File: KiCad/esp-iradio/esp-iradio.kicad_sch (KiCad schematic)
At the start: 0 parts

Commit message: KiCad: schematic on one A3 sheet in Elektuur style
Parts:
- added C1, C10, C12, C14, C22, C3, C5: 10uF, Capacitor_SMD:C_0805_2012Metric, symbol Elektuur:C
- added C11, C13, C17, C20, C21, C4, C6, C7, C8, C9: 100nF, Capacitor_SMD:C_0603_1608Metric, symbol Elektuur:C
- added C15, C16: 2.2uF, Capacitor_SMD:C_0603_1608Metric, symbol Elektuur:C
- added C18, C19: 2.2nF, Capacitor_SMD:C_0603_1608Metric, symbol Elektuur:C
- added C2, C23: 1uF, Capacitor_SMD:C_0603_1608Metric, symbol Elektuur:C
- added C24: 220uF 10V, Capacitor_SMD:CP_Elec_6.3x7.7, symbol Elektuur:C-polar
- added D1: SMAJ5.0CA, Diode_SMD:D_SMA, symbol Device:D_TVS
- added F1: 2A hold, Fuse:Fuse_1206_3216Metric, symbol Device:Polyfuse
- added FB1: 600R@100MHz, Inductor_SMD:L_0805_2012Metric, symbol Elektuur:L
- added FB2: 600R@100MHz 2A, Inductor_SMD:L_0805_2012Metric, symbol Elektuur:L
- added H1, H2, H3, H4: M3, MountingHole:MountingHole_3.2mm_M3, symbol Mechanical:MountingHole
- added J3: LCD 1.69in ST7789 (GND VCC SCL SDA RES DC CS BLK), Connector_PinSocket_2.54mm:PinSocket_1x08_P2.54mm_Vertical, symbol Connector_Generic:Conn_01x08
- added J4: microSD push-push, Connector_Card:microSD_HC_Hirose_DM3AT-SF-PEJM5, symbol Connector:Micro_SD_Card
- added J5: Line out 3.5mm, Connector_Audio:Jack_3.5mm_PJ320D_Horizontal, symbol Connector_Audio:AudioJack3
- added J6: Speaker 4-8 Ohm, Connector_JST:JST_PH_B2B-PH-K_1x02_P2.00mm_Vertical, symbol Connector_Generic:Conn_01x02
- added J7: USB-C power (GCT USB4125), Connector_USB:USB_C_Receptacle_GCT_USB4125-xx-x_6P_TopMnt_Horizontal, symbol Connector:USB_C_Receptacle_PowerOnly_6P
- added J8: Spare inputs, Connector_PinHeader_2.54mm:PinHeader_1x05_P2.54mm_Vertical, symbol Connector_Generic:Conn_01x05
- added MOD1: Olimex ESP32-DevKit-LiPo, esp-iradio:Olimex_ESP32-DevKit-LiPo_Socket, symbol esp-iradio:Olimex_ESP32-DevKit-LiPo
- added R1, R2: 5.1k 1%, Resistor_SMD:R_0603_1608Metric, symbol Elektuur:R
- added R10, R11, R12, R15, R3, R4, R5, R6, R7: 10k, Resistor_SMD:R_0603_1608Metric, symbol Elektuur:R
- added R13, R14: 10k DNP, Resistor_SMD:R_0603_1608Metric, symbol Elektuur:R
- added R16, R17: 470R, Resistor_SMD:R_0603_1608Metric, symbol Elektuur:R
- added R18, R19: 180k, Resistor_SMD:R_0603_1608Metric, symbol Elektuur:R
- added R20: 91k, Resistor_SMD:R_0603_1608Metric, symbol Elektuur:R
- added R21: 100k, Resistor_SMD:R_0603_1608Metric, symbol Elektuur:R
- added R8, R9: 0R, Resistor_SMD:R_0603_1608Metric, symbol Elektuur:R
- added SW1: EC11 with switch, Rotary_Encoder:RotaryEncoder_Alps_EC11E-Switch_Vertical_H20mm, symbol Device:RotaryEncoder_Switch
- added TP1: +5V_USBC, TestPoint:TestPoint_Pad_D1.5mm, symbol Connector:TestPoint
- added TP2: +VAMP, TestPoint:TestPoint_Pad_D1.5mm, symbol Connector:TestPoint
- added TP3: GND, TestPoint:TestPoint_Pad_D1.5mm, symbol Connector:TestPoint
- added TP4: +3V3, TestPoint:TestPoint_Pad_D1.5mm, symbol Connector:TestPoint
- added TP5: SPI_SCK, TestPoint:TestPoint_Pad_D1.5mm, symbol Connector:TestPoint
- added TP6: I2S_BCK, TestPoint:TestPoint_Pad_D1.5mm, symbol Connector:TestPoint
- added TP7: I2S_LRCK, TestPoint:TestPoint_Pad_D1.5mm, symbol Connector:TestPoint
- added TP8: I2S_DATA, TestPoint:TestPoint_Pad_D1.5mm, symbol Connector:TestPoint
- added U1: PCM5102APWR, Package_SO:TSSOP-20_4.4x6.5mm_P0.65mm, symbol Audio:PCM5102A
- added U2: PAM8302AASCR, Package_SO:SOIC-8_3.9x4.9mm_P1.27mm, symbol Amplifier_Audio:PAM8302AAS
- added U3: LM66100DCK, Package_TO_SOT_SMD:SOT-363_SC-70-6, symbol Power_Management:LM66100DCK
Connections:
- new net: MOD1.12 (IO14), TP7.1, U1.15 (LRCK)
- new net: J3.3 (Pin_3), J4.5 (CLK), R8.2 (-)
- new net: J3.4 (Pin_4), J4.3 (CMD), R9.2 (-)
- new net: J3.5 (Pin_5), MOD1.25 (IO21)
- new net: J3.6 (Pin_6), MOD1.22 (IO22)
- new net: J3.7 (Pin_7), MOD1.29 (IO5), R3.1 (+)
- new net: J3.8 (Pin_8), MOD1.10 (IO26)
- new net: J4.7 (DAT0), MOD1.27 (IO19), R5.1 (+)
- new net: C21.1 (+), R20.1 (+)
- new net: C6.1 (+), MOD1.7 (IO32), R10.2 (-), SW1.A
- new net: D1.2 (A2), F1.1, J7.A9 (VBUS), J7.B9 (VBUS)
- new net: MOD1.15 (IO13), TP8.1, U1.14 (DIN)
- new net: MOD1.28 (IO18), R8.1 (+), TP5.1
- new net: C7.1 (+), MOD1.8 (IO33), R11.2 (-), SW1.B
- new net: C8.1 (+), MOD1.9 (IO25), R12.2 (-), SW1.S1
- new net: MOD1.11 (IO27), TP6.1, U1.13 (BCK)
- new net: C19.1 (+), J5.R, R17.2 (-), R19.1 (+)
- new net: C18.1 (+), J5.T, R16.2 (-), R18.1 (+)
- new net: C15.1 (+), U1.2 (CAPP)
- new net: C15.2 (-), U1.4 (CAPM)
- new net: J4.1 (DAT2), R7.2 (-)
- new net: R15.2 (-), U1.17 (XSMT)
- new net: C17.1 (+), U1.18 (LDOO)
- new net: C16.1 (+), U1.5 (VNEG)
- new net: R16.1 (+), U1.6 (OUTL)
- new net: R17.1 (+), U1.7 (OUTR)
- new net: C20.1 (+), R18.2 (-), R19.2 (-)
- new net: MOD1.34 (IO2), R21.1 (+), U2.1 (~{SD})
- new net: C20.2 (-), U2.3 (IN+)
- new net: R20.2 (-), U2.4 (IN-)
- new net: J6.1 (Pin_1), U2.5 (OUT+)
- new net: J6.2 (Pin_2), U2.8 (OUT-)
- new net: J7.A5 (CC1), R1.1 (+)
- new net: J7.B5 (CC2), R2.1 (+)
- new net: J4.8 (DAT1), R6.1 (+)
- new net: MOD1.21 (IO23), R9.1 (+)
- new net: J4.2 (DAT3/CD), MOD1.32 (IO4), R4.2 (-)
- new net: J8.2 (Pin_2), MOD1.5 (IO34), R13.1 (+)
- new net: J8.3 (Pin_3), MOD1.3 (IO36), R14.2 (-)
- new net +3V3: C10.1 (+), C11.1 (+), C12.1 (+), C3.1 (+), C4.1 (+), C5.1 (+), C9.1 (+), FB1.1 (+), J3.2 (Pin_2), J4.4 (VDD), J8.1 (Pin_1), MOD1.1 (3V3), R10.1 (+), R11.1 (+), R12.1 (+), R13.2 (-), R14.1 (+), R15.1 (+), R3.2 (-), R4.1 (+), R5.2 (-), R6.2 (-), R7.1 (+), TP4.1, U1.1 (CPVDD), U1.20 (DVDD)
- new net +3V3A: C13.1 (+), C14.1 (+), FB1.2 (-), U1.8 (AVDD)
- new net +5V_OLI: C2.1 (+), MOD1.19 (5V), U3.6 (VOUT)
- new net +5V_USBC: C1.1 (+), F1.2, FB2.1 (+), TP1.1, U3.1 (VIN)
- new net +VAMP: C22.1 (+), C23.1 (+), C24.1 (+), FB2.2 (-), TP2.1, U2.6 (VDD)
- new net GND: C1.2 (-), C10.2 (-), C11.2 (-), C12.2 (-), C13.2 (-), C14.2 (-), C16.2 (-), C17.2 (-), C18.2 (-), C19.2 (-), C2.2 (-), C21.2 (-), C22.2 (-), C23.2 (-), C24.2 (-), C3.2 (-), C4.2 (-), C5.2 (-), C6.2 (-), C7.2 (-), C8.2 (-), C9.2 (-), D1.1 (A1), J3.1 (Pin_1), J4.6 (VSS), J4.9 (SHIELD), J5.S, J7.A12 (GND), J7.B12 (GND), J7.S1 (SHIELD), J8.4 (Pin_4), J8.5 (Pin_5), MOD1.14 (GND), MOD1.20 (GND), MOD1.26 (GND), R1.2 (-), R2.2 (-), R21.2 (-), SW1.C, SW1.S2, TP3.1, U1.10 (DEMP), U1.11 (FLT), U1.12 (SCK), U1.16 (FMT), U1.19 (DGND), U1.3 (CPGND), U1.9 (AGND), U2.7 (GND), U3.2 (GND), U3.3 (~{CE})
- no-connect marks 0 -> 19
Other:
- removed sheet Audio
- removed sheet Controls
- removed sheet Display and microSD
- removed sheet Olimex socket
- removed sheet Power
- note added: "AUDIO: PCM5102A DAC, 3.5 mm line out, PAM8302A mono amplifier"
- note added: "CONTROLS: EC11 encoder, spare inputs"
- note added: "DISPLAY (ST7789, SPI) AND microSD"
- note added: "POWER: USB-C 5 V in, ideal diode to the Olimex 5 V pin"
- company: (none) -> hghaken
- title: (none) -> ESP iRadio carrier board

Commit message: KiCad: R8 22 Ohm series resistor on SPI SCK
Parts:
- R8: value 0R -> 22R
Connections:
- net +3V3: now also R13.1 (+); no longer R13.2 (-)
- net at J8.2 (Pin_2), MOD1.5 (IO34): now also R13.2 (-); no longer R13.1 (+)
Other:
- moved on the sheet: R1, R13, R14, TP3

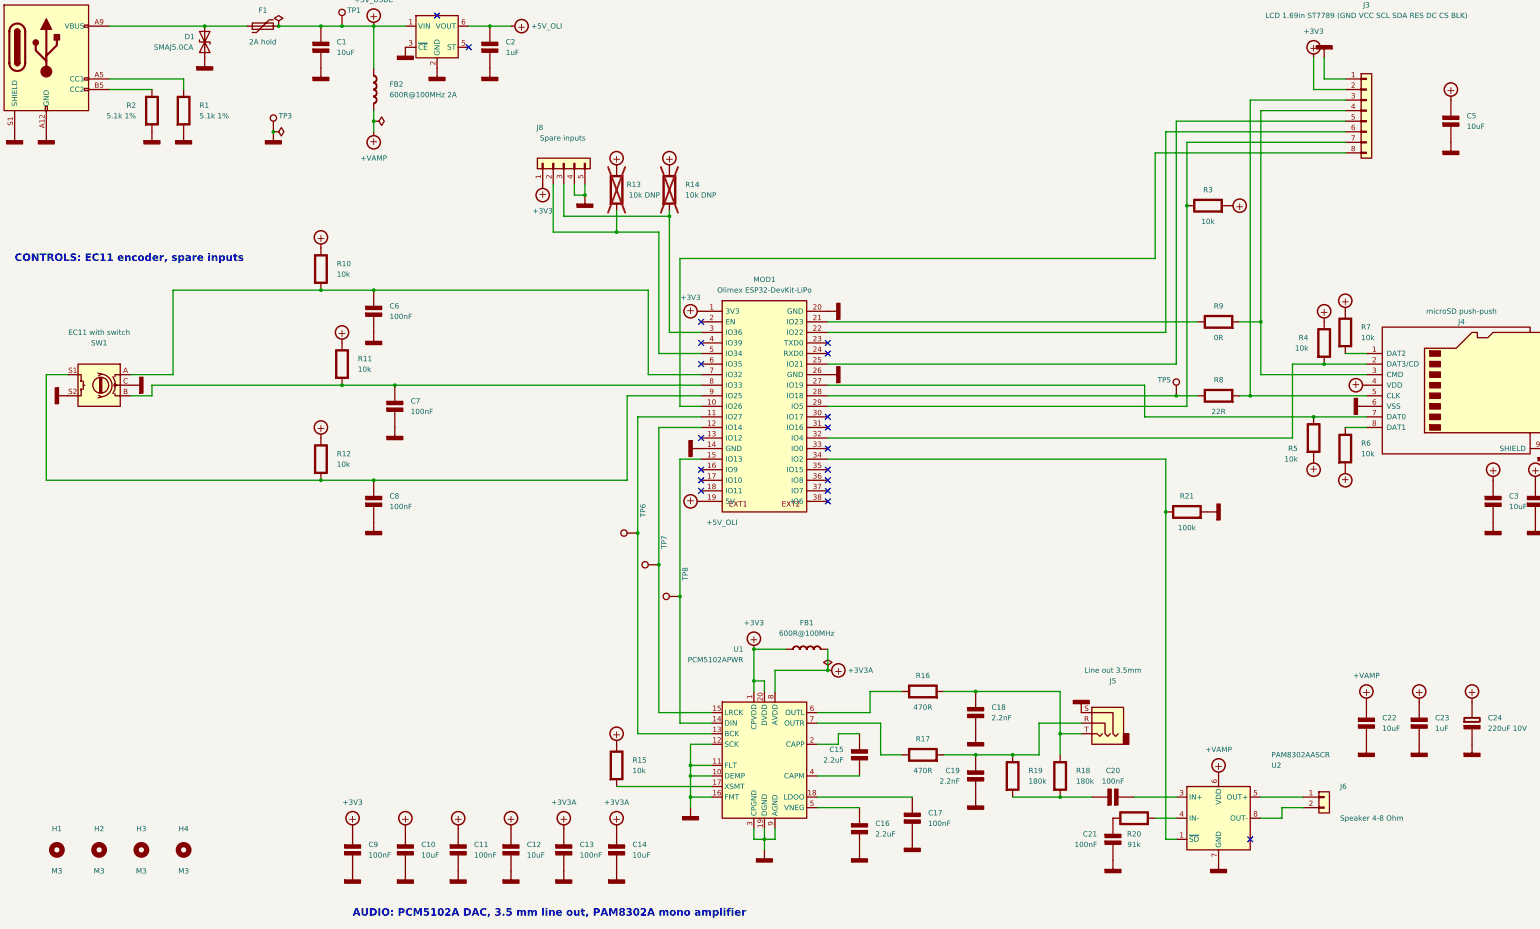
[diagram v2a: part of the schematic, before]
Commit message: KiCad: MAX98357A I2S amplifier instead of the PAM8302A
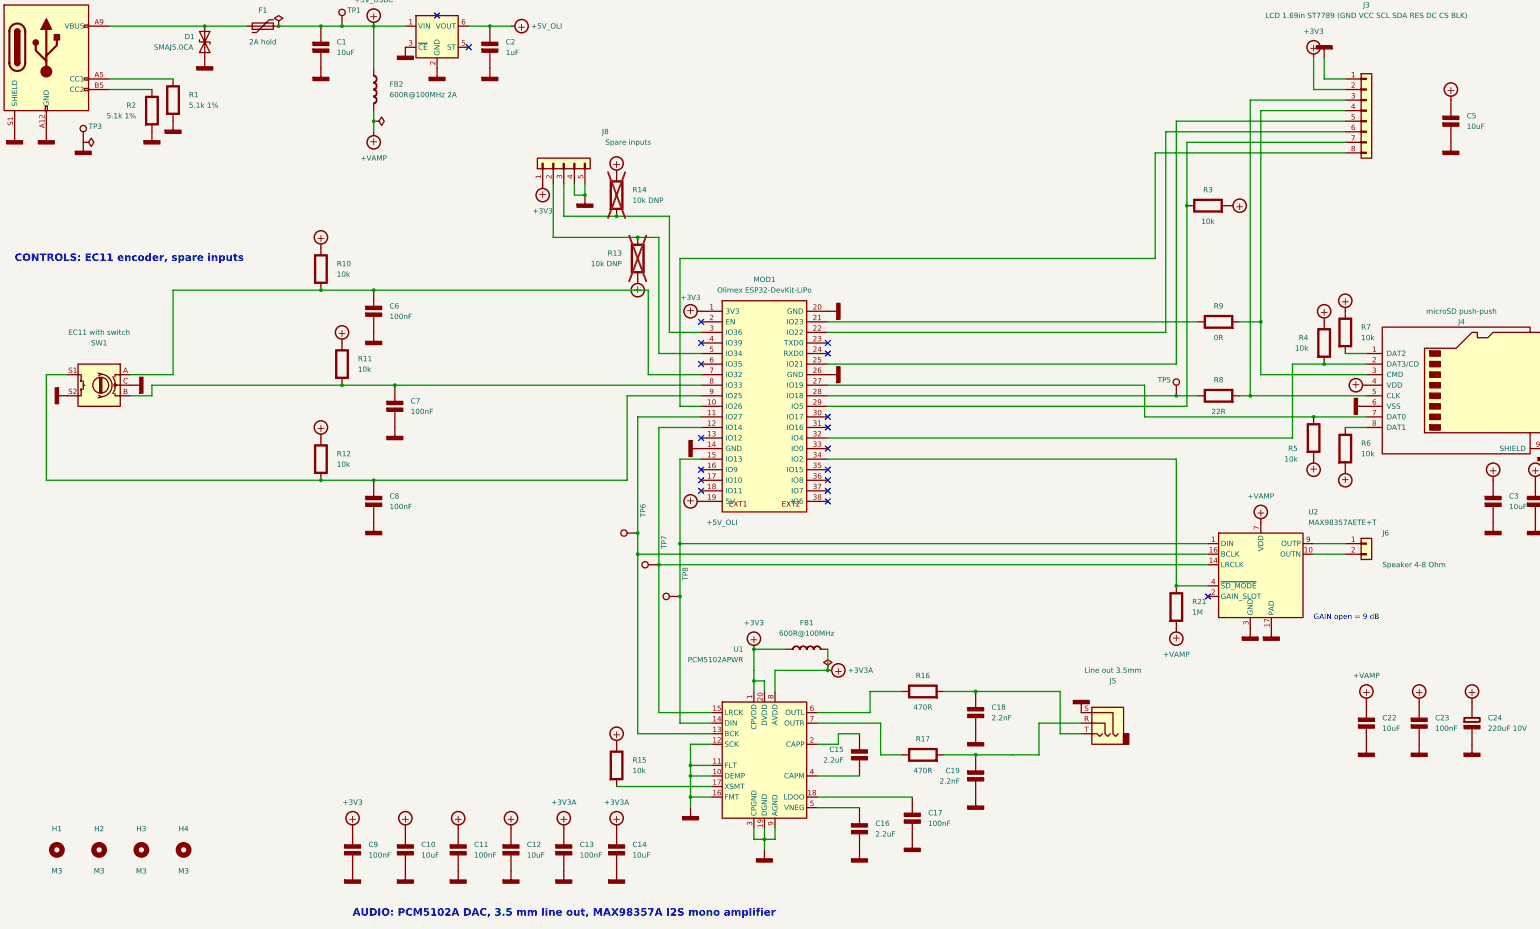
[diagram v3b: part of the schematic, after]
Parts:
- removed C20, C21: 100nF, Capacitor_SMD:C_0603_1608Metric, symbol Elektuur:C
- removed R18, R19: 180k, Resistor_SMD:R_0603_1608Metric, symbol Elektuur:R
- removed R20: 91k, Resistor_SMD:R_0603_1608Metric, symbol Elektuur:R
- removed U2: PAM8302AASCR, Package_SO:SOIC-8_3.9x4.9mm_P1.27mm, symbol Amplifier_Audio:PAM8302AAS
- added U2: MAX98357AETE+T, Package_DFN_QFN:TQFN-16-1EP_3x3mm_P0.5mm_EP1.23x1.23mm, symbol Audio:MAX98357A
- C23: value 1uF -> 100nF
- R21: value 100k -> 1M
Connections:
- net +3V3: now also R13.2 (-); no longer R13.1 (+)
- net +VAMP: now also R21.2 (-), U2.7 (VDD), U2.8 (VDD)
- net GND: now also U2.11 (GND), U2.15 (GND), U2.17 (PAD), U2.3 (GND); no longer R21.2 (-)
- net at MOD1.12 (IO14), TP7.1, U1.15 (LRCK): now also U2.14 (LRCLK)
- net at MOD1.15 (IO13), TP8.1, U1.14 (DIN): now also U2.1 (DIN)
- net at MOD1.11 (IO27), TP6.1, U1.13 (BCK): now also U2.16 (BCLK)
- net at MOD1.34 (IO2), R21.1 (+): now also U2.4 (~{SD_MODE})
- net at J6.1 (Pin_1): now also U2.9 (OUTP)
- net at J6.2 (Pin_2): now also U2.10 (OUTN)
- net at J8.2 (Pin_2), MOD1.5 (IO34): now also R13.1 (+); no longer R13.2 (-)
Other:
- note added: "AUDIO: PCM5102A DAC, 3.5 mm line out, MAX98357A I2S mono amplifier"
- note added: "GAIN open = 9 dB"
- note removed: "AUDIO: PCM5102A DAC, 3.5 mm line out, PAM8302A mono amplifier"
